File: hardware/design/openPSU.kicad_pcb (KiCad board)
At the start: 2 copper layers, 100 x 50 mm, 85 parts, among them Q1 BC846B, Q2 BCP54, Q3 BC857A, U1 ADR02ARZ, U2 MC34071, U3 MC34071

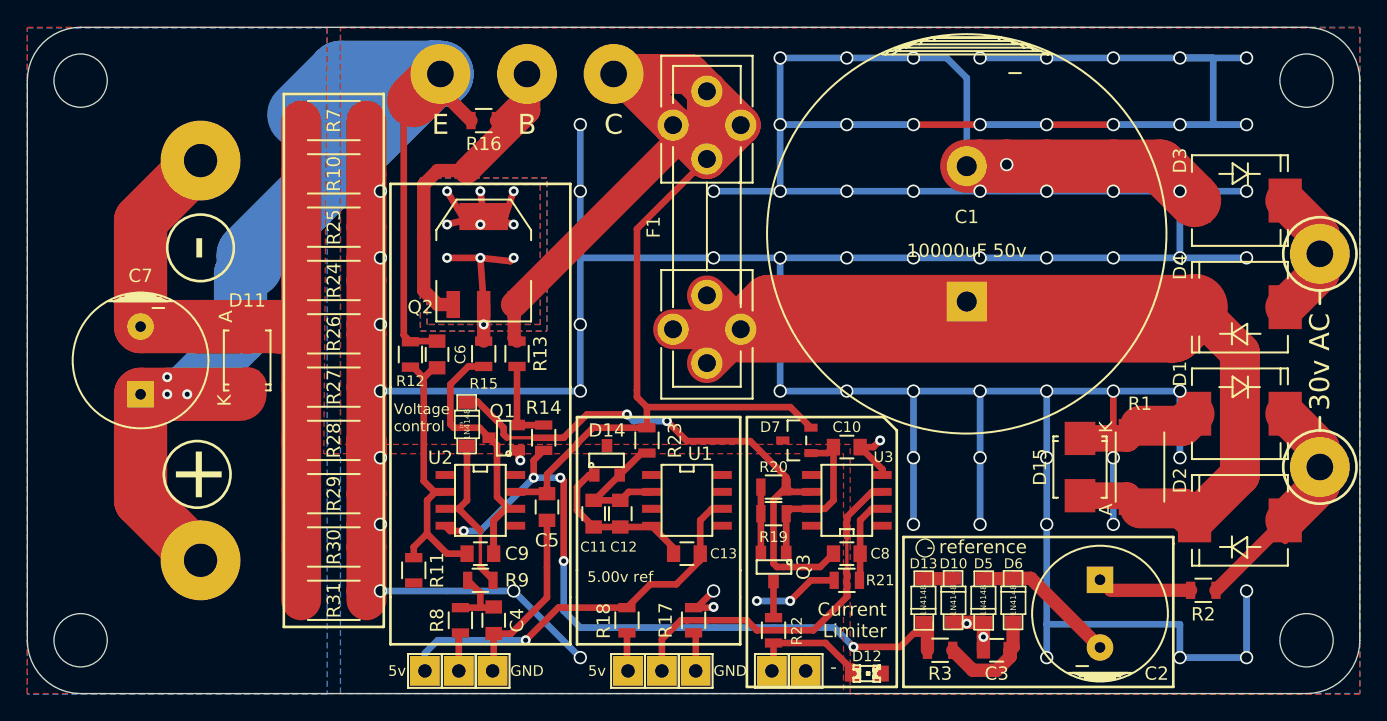
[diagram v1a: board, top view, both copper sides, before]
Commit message: Fixed transistors and zeners pinouts. Added the last connector so we can stack a digital board on top. It could support a display, communications, programmable voltage and datalogging. Added manufacturing files sent to itead studio
Signed-off-by: Marcos Chaparro <marcos@mrkindustries.com.ar>
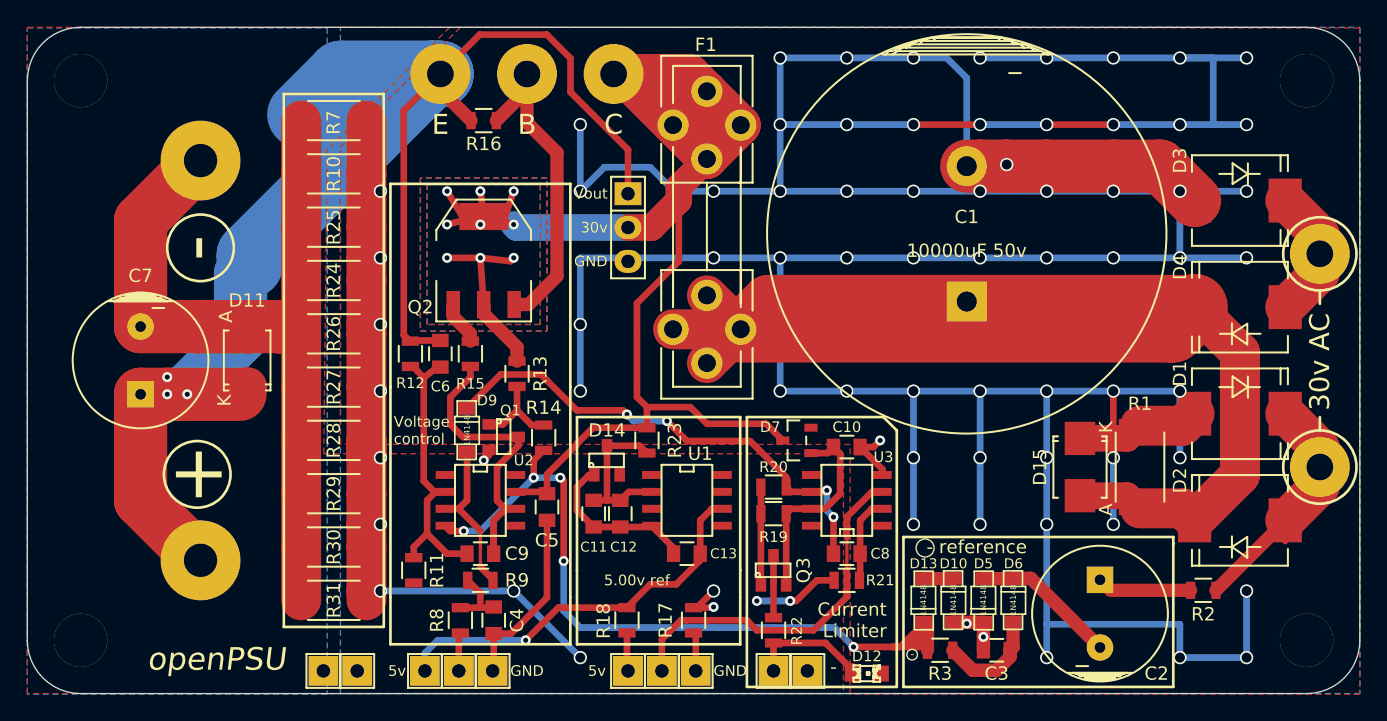
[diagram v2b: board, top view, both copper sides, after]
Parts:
- added CONN5: SHUNT-, Socket_Strips:Socket_Strip_Straight_1x01, F.Cu at (111.8, 114.3)
- added CONN6: SHUNT+, Socket_Strips:Socket_Strip_Straight_1x01, F.Cu at (109.2, 114.3)
- added P3: Monitor, Socket_Strips:Socket_Strip_Straight_1x03, F.Cu at (132.1, 81.0)
- C3: value 47uF 100v -> 47uF
- C5: value 200nF -> 100nF
- D11: value 1N4001 -> SS1200-LTP
- D14, D7: value ZENER -> 6.8v ZENER
- R22: value 4.7k 1/4W -> 1k 1/4W
- moved G*** 45.6 mm to (96.0, 67.8)
- moved R13 1.50 mm to (123.8, 92.0)
- moved R15 1.00 mm to (120.2, 90.5)
- moved D9 0.45 mm to (120.0, 96.2)
- moved C6 0.25 mm to (118.0, 90.5)
- moved Q3 0.25 mm to (143.0, 106.8), turned to 0 degrees
- moved CONN_LED2 0.13 mm to (145.5, 114.3)
- moved CONN_LED1 0.13 mm to (143.0, 114.3)
- turned Q1 to 270 degrees
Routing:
- net /30v: track 103.2 -> 127.3 mm, vias 0 -> 9
- net Net-(Q2-Pad2): track 26.5 -> 4.02 mm, vias 10 -> 0
- net /Vout: track 128.6 -> 149.6 mm
- net GND: track 515.0 -> 505.8 mm
- net /-5.6v: track 54.0 -> 58.9 mm
- net Net-(C8-Pad2): track 42.0 -> 37.2 mm, vias 2 -> 4
- net Net-(CONN8-Pad1): track 30.1 -> 25.9 mm
- net Net-(C10-Pad1): track 12.7 -> 15.6 mm
- net Net-(C11-Pad1): track 10.1 -> 12.9 mm
- net Net-(Q3-Pad2): track 4.90 -> 7.35 mm
- net Net-(Q3-Pad3): track 2.70 -> 4.65 mm
- net Net-(C9-Pad1): track 24.3 -> 25.7 mm
- added copper zone on B.Cu, net /30v
- added copper zone on F.Cu, net /30v
- removed copper zone on B.Cu, net Net-(Q2-Pad2)
- removed copper zone on F.Cu, net Net-(Q2-Pad2)
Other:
- board text added: "30v"
- board text added: "OC+"
- board text added: "OC-"
- board text added: "SH+"
- board text added: "SH-"
- board text added: "Vout"
- board text added: "openPSU"

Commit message: Created a one-click digikey BOM, enlarged output pads and minor changes. The order was rejected from iteadstudio due to the extended attributes in kicad gerber file. Its now corrected and the production continued with this changes incorporated.
Signed-off-by: Marcos Chaparro <marcos@mrkindustries.com.ar>
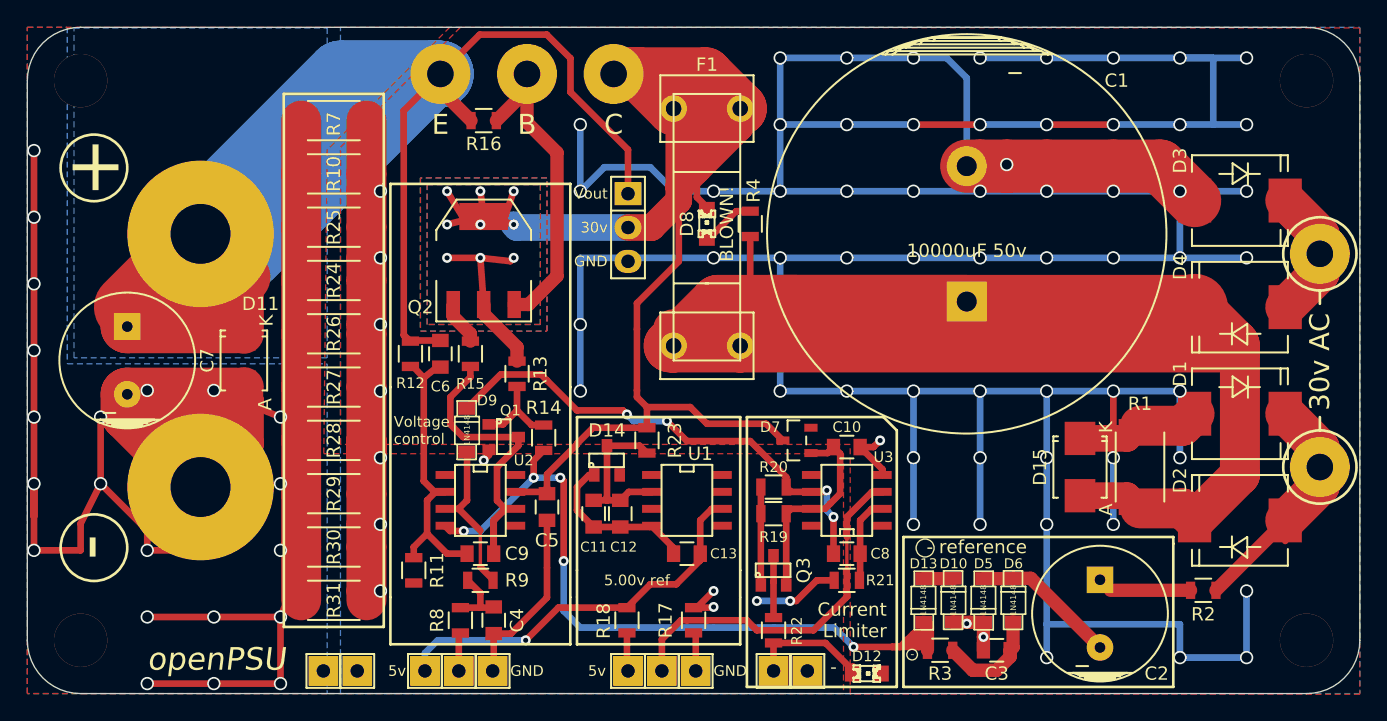
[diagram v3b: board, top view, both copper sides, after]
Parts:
- removed the G*** at (153.4, 98.5)
- removed the G*** at (96.0, 67.8)
- removed Symbol_OSHW-Logo_SilkScreen_BIG: VAL**, Symbols:Symbol_OSHW-Logo_SilkScreen_BIG
- added D8: BLOWN, LEDs:LED-0805, F.Cu at (138.0, 80.8)
- added R4: 1k 1/4W, Resistors_SMD:R_0805, F.Cu at (141.2, 80.8)
- moved CONN3 24.5 mm to (100.0, 81.5)
- moved CONN4 24.5 mm to (100.0, 100.5)
- moved C7 1.00 mm to (94.5, 91.0), turned to 180 degrees
- moved D11 0.25 mm to (103.2, 91.0), turned to 90 degrees
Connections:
- net /-5.6v renamed /-V
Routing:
- net /GNDout: track 97.4 -> 216.6 mm, vias 2 -> 23
- net Net-(C1-Pad1): track 110.3 -> 184.2 mm
- net /Vout: track 149.6 -> 170.1 mm, vias 3 -> 0
- net /30v: track 127.3 -> 147.0 mm
- net GND: track 505.8 -> 488.7 mm, vias 74 -> 72
- net Net-(D8-Pad1): track 0.00 -> 4.08 mm
- added copper zone on B.Cu, net /GNDout
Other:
- board text added: "BLOWN!"

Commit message: Very minor changes
Signed-off-by: Marcos Chaparro <marcos@mrkindustries.com.ar>
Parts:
- added Symbol_OSHW-Logo_SilkScreen_BIG: VAL**, Symbols:Symbol_OSHW-Logo_SilkScreen_BIG, B.Cu at (191.5, 90.5)
- turned C2 to 90 degrees
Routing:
- net GND: track 488.7 -> 493.3 mm, vias 72 -> 75
- net Net-(C2-Pad2): track 10.9 -> 7.29 mm
- net Net-(C2-Pad1): track 7.13 -> 4.98 mm
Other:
- board text added: "0v"
